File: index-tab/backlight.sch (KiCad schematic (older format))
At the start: 0 parts

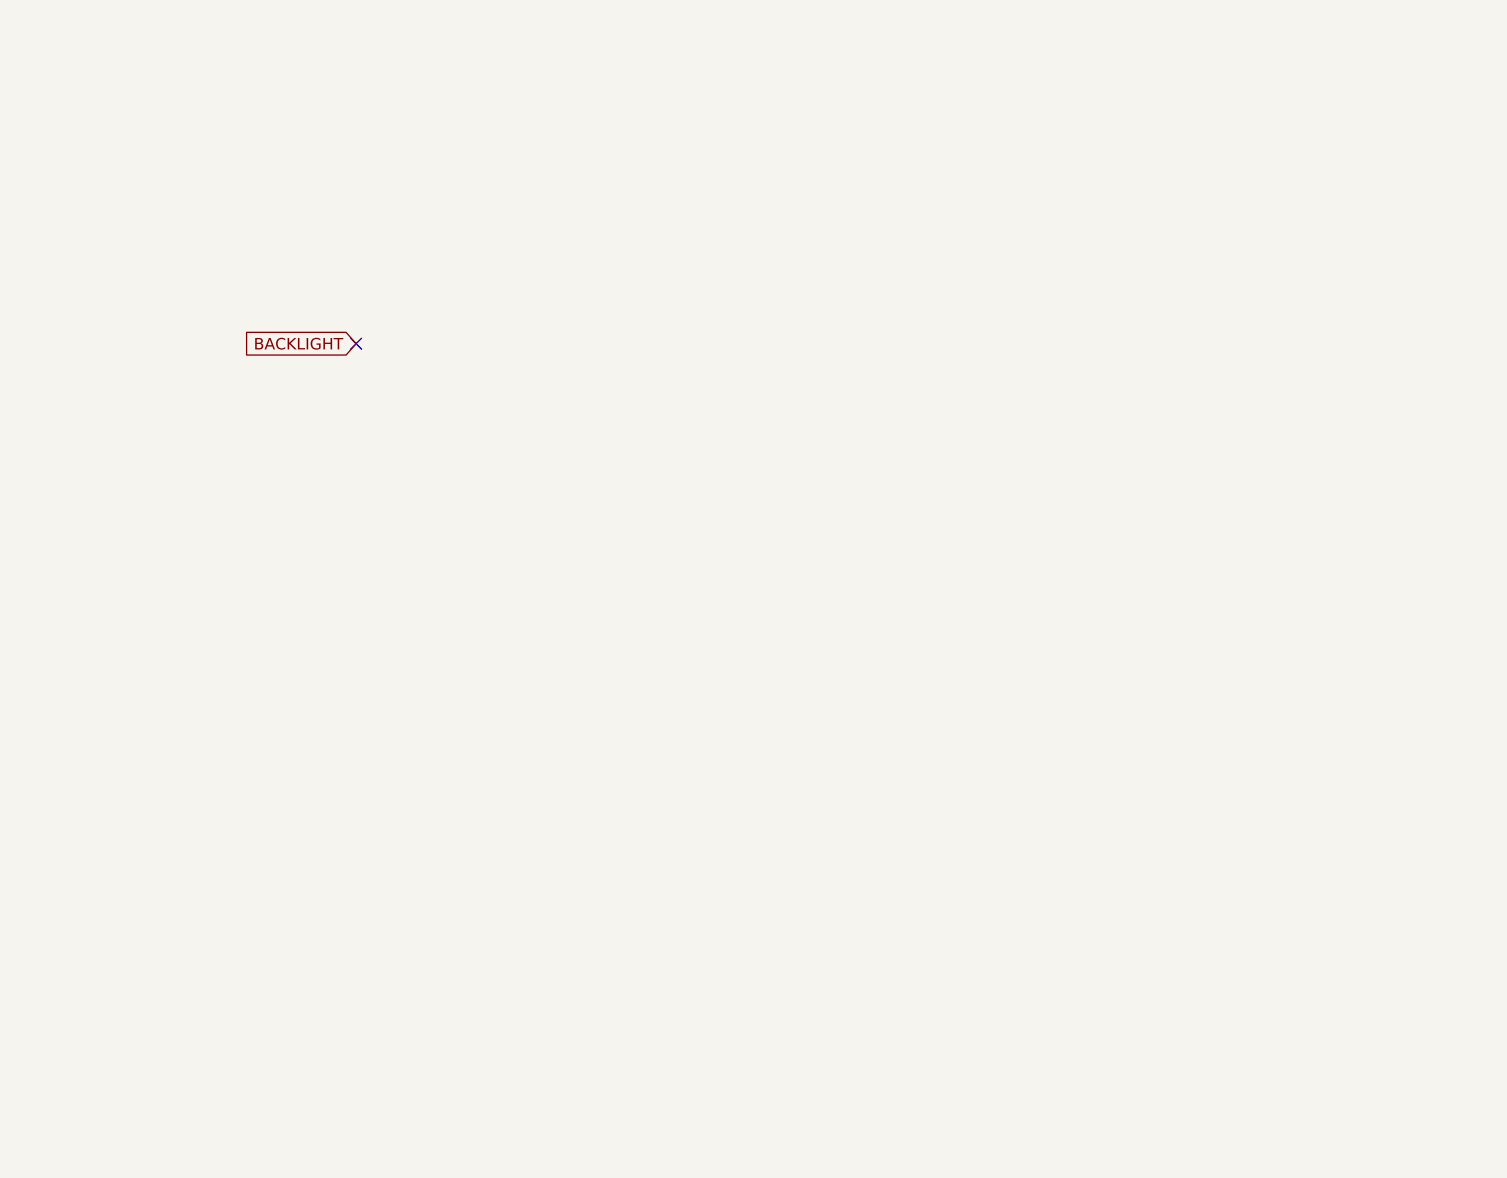
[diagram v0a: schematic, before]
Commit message: added backlight and rgb
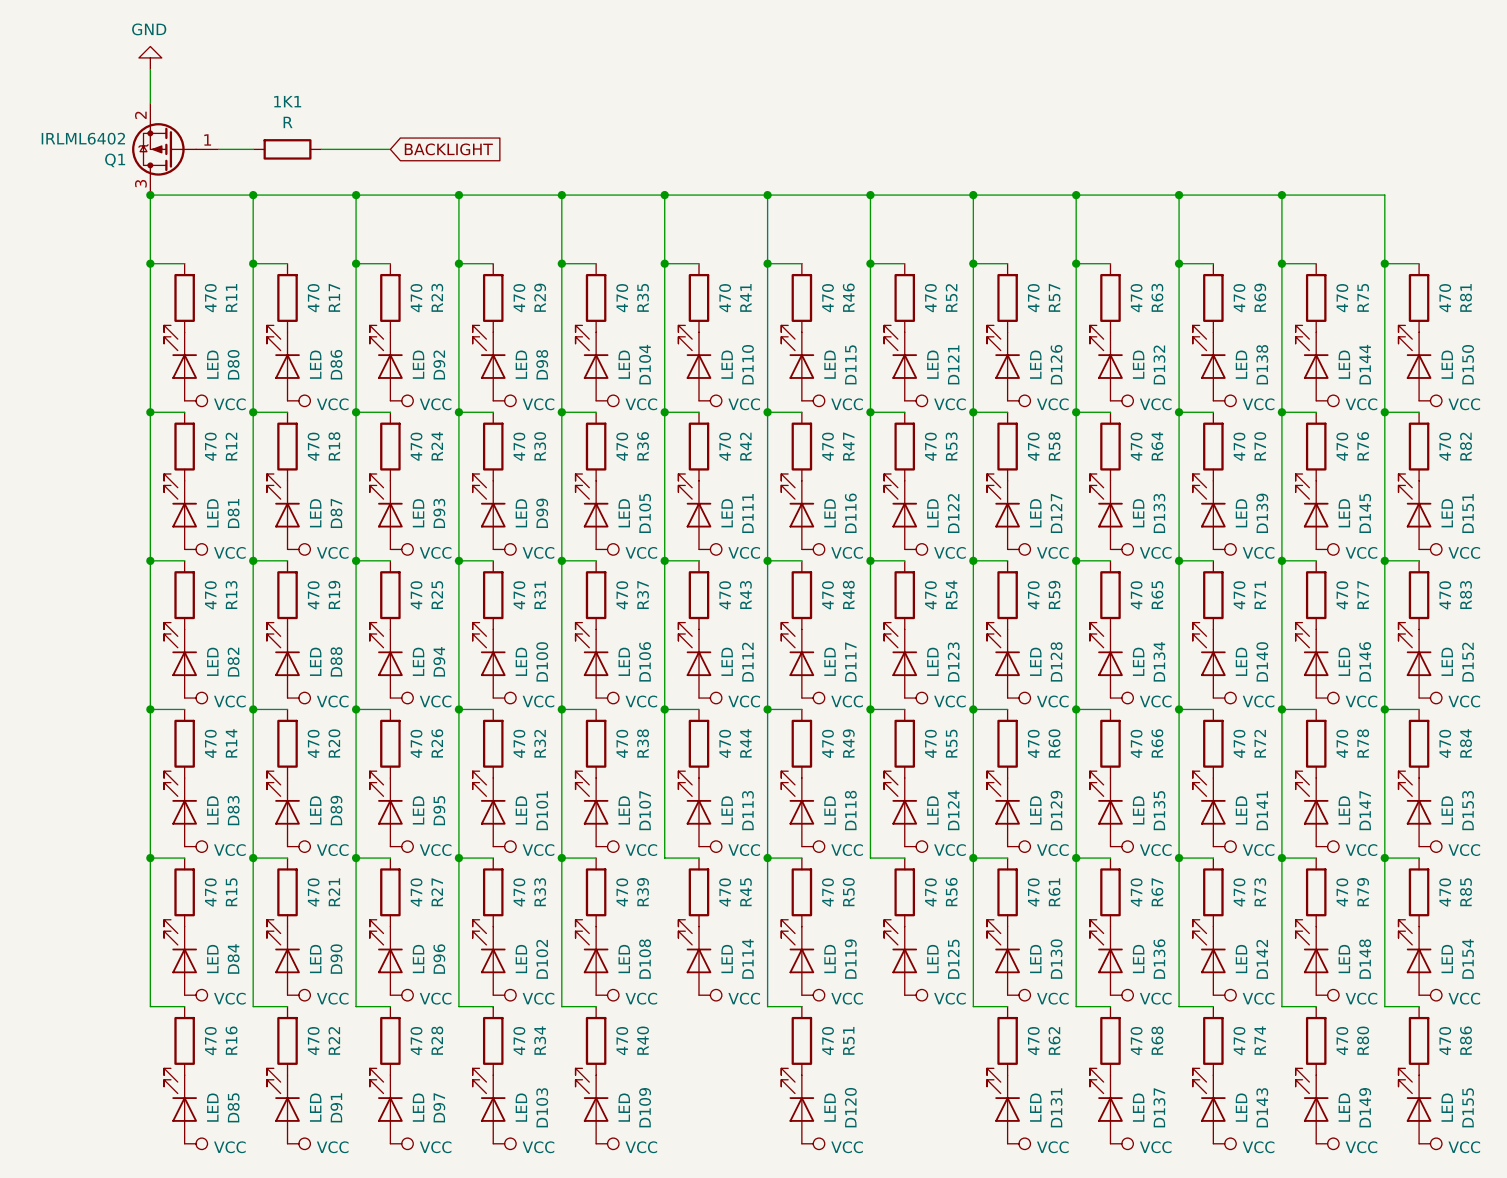
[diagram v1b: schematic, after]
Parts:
- added 1K1: R, symbol Device:R
- added D100, D101, D102, D103, D104, D105, D106, D107, D108, D109, D110, D111, D112, D113, D114, D115, D116, D117, D118, D119, D120, D121, D122, D123, D124, D125, D126, D127, D128, D129, D130, D131, D132, D133, D134, D135, D136, D137, D138, D139, D140, D141, D142, D143, D144, D145, D146, D147, D148, D149, D150, D151, D152, D153, D154, D155, D80, D81, D82, D83, D84, D85, D86, D87, D88, D89, D90, D91, D92, D93, D94, D95, D96, D97, D98, D99: LED, symbol Device:LED
- added Q1: IRLML6402, Package_TO_SOT_SMD:SOT-23, symbol Transistor_FET:IRLML6402
- added R11, R12, R13, R14, R15, R16, R17, R18, R19, R20, R21, R22, R23, R24, R25, R26, R27, R28, R29, R30, R31, R32, R33, R34, R35, R36, R37, R38, R39, R40, R41, R42, R43, R44, R45, R46, R47, R48, R49, R50, R51, R52, R53, R54, R55, R56, R57, R58, R59, R60, R61, R62, R63, R64, R65, R66, R67, R68, R69, R70, R71, R72, R73, R74, R75, R76, R77, R78, R79, R80, R81, R82, R83, R84, R85, R86: 470, symbol Device:R
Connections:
- net BACKLIGHT: now also 1K1.1
- new net: 1K1.2, Q1.1 (G)
- new net: Q1.3 (D), R11.2, R12.2, R13.2, R14.2, R15.2, R16.2, R17.2, R18.2, R19.2, R20.2, R21.2, R22.2, R23.2, R24.2, R25.2, R26.2, R27.2, R28.2, R29.2, R30.2, R31.2, R32.2, R33.2, R34.2, R35.2, R36.2, R37.2, R38.2, R39.2, R40.2, R41.2, R42.2, R43.2, R44.2, R45.2, R46.2, R47.2, R48.2, R49.2, R50.2, R51.2, R52.2, R53.2, R54.2, R55.2, R56.2, R57.2, R58.2, R59.2, R60.2, R61.2, R62.2, R63.2, R64.2, R65.2, R66.2, R67.2, R68.2, R69.2, R70.2, R71.2, R72.2, R73.2, R74.2, R75.2, R76.2, R77.2, R78.2, R79.2, R80.2, R81.2, R82.2, R83.2, R84.2, R85.2, R86.2
- new net: D80.1 (K), R11.1
- new net: D81.1 (K), R12.1
- new net: D82.1 (K), R13.1
- new net: D83.1 (K), R14.1
- new net: D84.1 (K), R15.1
- new net: D85.1 (K), R16.1
- new net: D86.1 (K), R17.1
- new net: D87.1 (K), R18.1
- new net: D88.1 (K), R19.1
- new net: D89.1 (K), R20.1
- new net: D90.1 (K), R21.1
- new net: D91.1 (K), R22.1
- new net: D92.1 (K), R23.1
- new net: D93.1 (K), R24.1
- new net: D94.1 (K), R25.1
- new net: D95.1 (K), R26.1
- new net: D96.1 (K), R27.1
- new net: D97.1 (K), R28.1
- new net: D98.1 (K), R29.1
- new net: D99.1 (K), R30.1
- new net: D100.1 (K), R31.1
- new net: D101.1 (K), R32.1
- new net: D102.1 (K), R33.1
- new net: D103.1 (K), R34.1
- new net: D104.1 (K), R35.1
- new net: D105.1 (K), R36.1
- new net: D106.1 (K), R37.1
- new net: D107.1 (K), R38.1
- new net: D108.1 (K), R39.1
- new net: D109.1 (K), R40.1
- new net: D110.1 (K), R41.1
- new net: D111.1 (K), R42.1
- new net: D112.1 (K), R43.1
- new net: D113.1 (K), R44.1
- new net: D114.1 (K), R45.1
- new net: D115.1 (K), R46.1
- new net: D116.1 (K), R47.1
- new net: D117.1 (K), R48.1
- new net: D118.1 (K), R49.1
- new net: D119.1 (K), R50.1
- new net: D120.1 (K), R51.1
- new net: D121.1 (K), R52.1
- new net: D122.1 (K), R53.1
- new net: D123.1 (K), R54.1
- new net: D124.1 (K), R55.1
- new net: D125.1 (K), R56.1
- new net: D126.1 (K), R57.1
- new net: D127.1 (K), R58.1
- new net: D128.1 (K), R59.1
- new net: D129.1 (K), R60.1
- new net: D130.1 (K), R61.1
- new net: D131.1 (K), R62.1
- new net: D132.1 (K), R63.1
- new net: D133.1 (K), R64.1
- new net: D134.1 (K), R65.1
- new net: D135.1 (K), R66.1
- new net: D136.1 (K), R67.1
- new net: D137.1 (K), R68.1
- new net: D138.1 (K), R69.1
- new net: D139.1 (K), R70.1
- new net: D140.1 (K), R71.1
- new net: D141.1 (K), R72.1
- new net: D142.1 (K), R73.1
- new net: D143.1 (K), R74.1
- new net: D144.1 (K), R75.1
- new net: D145.1 (K), R76.1
- new net: D146.1 (K), R77.1
- new net: D147.1 (K), R78.1
- new net: D148.1 (K), R79.1
- new net: D149.1 (K), R80.1
- new net: D150.1 (K), R81.1
- new net: D151.1 (K), R82.1
- new net: D152.1 (K), R83.1
- new net: D153.1 (K), R84.1
- new net: D154.1 (K), R85.1
- new net: D155.1 (K), R86.1
- new net GND: Q1.2 (S)
- new net VCC: D100.2 (A), D101.2 (A), D102.2 (A), D103.2 (A), D104.2 (A), D105.2 (A), D106.2 (A), D107.2 (A), D108.2 (A), D109.2 (A), D110.2 (A), D111.2 (A), D112.2 (A), D113.2 (A), D114.2 (A), D115.2 (A), D116.2 (A), D117.2 (A), D118.2 (A), D119.2 (A), D120.2 (A), D121.2 (A), D122.2 (A), D123.2 (A), D124.2 (A), D125.2 (A), D126.2 (A), D127.2 (A), D128.2 (A), D129.2 (A), D130.2 (A), D131.2 (A), D132.2 (A), D133.2 (A), D134.2 (A), D135.2 (A), D136.2 (A), D137.2 (A), D138.2 (A), D139.2 (A), D140.2 (A), D141.2 (A), D142.2 (A), D143.2 (A), D144.2 (A), D145.2 (A), D146.2 (A), D147.2 (A), D148.2 (A), D149.2 (A), D150.2 (A), D151.2 (A), D152.2 (A), D153.2 (A), D154.2 (A), D155.2 (A), D80.2 (A), D81.2 (A), D82.2 (A), D83.2 (A), D84.2 (A), D85.2 (A), D86.2 (A), D87.2 (A), D88.2 (A), D89.2 (A), D90.2 (A), D91.2 (A), D92.2 (A), D93.2 (A), D94.2 (A), D95.2 (A), D96.2 (A), D97.2 (A), D98.2 (A), D99.2 (A)
- no-connect marks 1 -> 0

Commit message: Added footprints to all components, and done some formatting
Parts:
- 1K1, R11, R12, R13, R14, R15, R16, R17, R18, R19, R20, R21, R22, R23, R24, R25, R26, R27, R28, R29, R30, R31, R32, R33, R34, R35, R36, R37, R38, R39, R40, R41, R42, R43, R44, R45, R46, R47, R48, R49, R50, R51, R52, R53, R54, R55, R56, R57, R58, R59, R60, R61, R62, R63, R64, R65, R66, R67, R68, R69, R70, R71, R72, R73, R74, R75, R76, R77, R78, R79, R80, R81, R82, R83, R84, R85, R86: footprint (none) -> Resistor_SMD:R_0201_0603Metric
- D100, D101, D102, D103, D104, D105, D106, D107, D108, D109, D110, D111, D112, D113, D114, D115, D116, D117, D118, D119, D120, D121, D122, D123, D124, D125, D126, D127, D128, D129, D130, D131, D132, D133, D134, D135, D136, D137, D138, D139, D140, D141, D142, D143, D144, D145, D146, D147, D148, D149, D150, D151, D152, D153, D154, D155, D80, D81, D82, D83, D84, D85, D86, D87, D88, D89, D90, D91, D92, D93, D94, D95, D96, D97, D98, D99: footprint (none) -> LED_THT:LED_D3.0mm_FlatTop
